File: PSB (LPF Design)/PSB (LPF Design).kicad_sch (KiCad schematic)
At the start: 18 parts, among them J1 Screw_Terminal_01x02, U1 TL081, U2 TL081

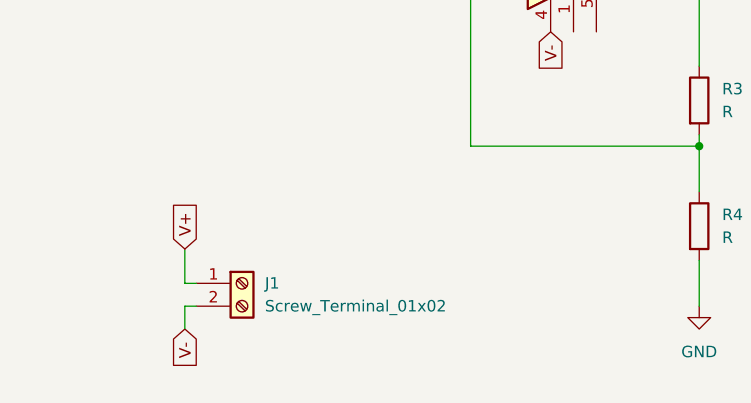
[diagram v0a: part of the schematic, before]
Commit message: third revision(forgot the resistor)
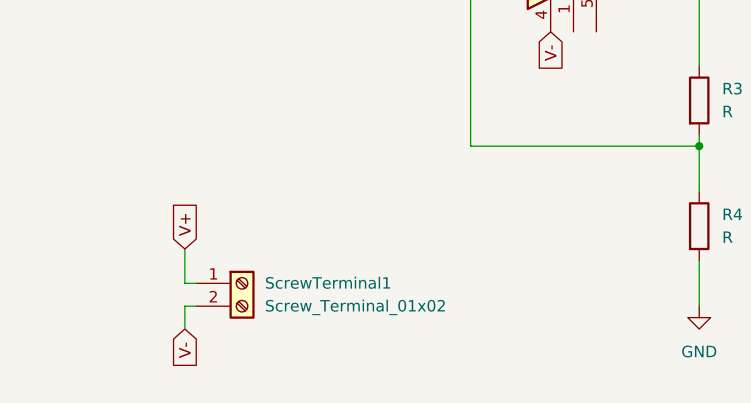
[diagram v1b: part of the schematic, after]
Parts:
- C1, C2, C3, C4: footprint Capacitor_THT:C_Disc_D5.0mm_W2.5mm_P2.50mm -> Capacitor_THT:C_Rect_L18.0mm_W6.0mm_P15.00mm_FKS3_FKP3
- renumbered J1 to ScrewTerminal1
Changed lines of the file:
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@@
 			)
 		)
-		(property "Footprint" "Capacitor_THT:C_Disc_D5.0mm_W2.5mm_P2.50mm"
+		(property "Footprint" "Capacitor_THT:C_Rect_L18.0mm_W6.0mm_P15.00mm_FKS3_FKP3"
 			(at 168.6052 74.93 0)
 			(effects
@@
 		(dnp no)
 		(fields_autoplaced yes)
-		(property "Reference" "J1"
+		(property "Reference" "ScrewTerminal1"
 			(at 104.14 118.1099 0)
 			(effects
@@
 			(project ""
 				(path "/084b7188-85fa-49c4-936c-1f04d12cf3f4"
-					(reference "J1")
+					(reference "ScrewTerminal1")
 					(unit 1)
 				)
@@
 			)
 		)
-		(property "Footprint" "Capacitor_THT:C_Disc_D5.0mm_W2.5mm_P2.50mm"
+		(property "Footprint" "Capacitor_THT:C_Rect_L18.0mm_W6.0mm_P15.00mm_FKS3_FKP3"
 			(at 94.9452 68.58 0)
 			(effects
@@
 			)
 		)
-		(property "Footprint" "Capacitor_THT:C_Disc_D5.0mm_W2.5mm_P2.50mm"
+		(property "Footprint" "Capacitor_THT:C_Rect_L18.0mm_W6.0mm_P15.00mm_FKS3_FKP3"
 			(at 121.6152 68.58 0)
 			(effects
@@
 			)
 		)
-		(property "Footprint" "Capacitor_THT:C_Disc_D5.0mm_W2.5mm_P2.50mm"
+		(property "Footprint" "Capacitor_THT:C_Rect_L18.0mm_W6.0mm_P15.00mm_FKS3_FKP3"
 			(at 188.9252 74.93 0)
 			(effects
